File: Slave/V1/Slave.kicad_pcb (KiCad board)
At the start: 2 copper layers, 130.6 x 138.2 mm, 534 parts, among them J101 649002227222, J102 649002227222, J1301 649002227222, J1701 649002227222, J201 Header_Male_Pin_2.54mm_1X6_,_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, J202 Header_Male_Pin_2.54mm_1X3_,_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, J2101 649002227222, J2501 649002227222, J2901 649002227222, J300 Header_Male_Pin_2.54mm_1X2_,_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, J3301 649002227222, J401 649006227222, J402 649006227222, J501 649002227222, J901 649002227222, Q101 2N7002P,215, Q1201 CPH6347-TL-W, Q1202 BSS806NH6327XTSA1, Q1301 CPH6347-TL-W, Q1302 CPH6347-TL-W, Q1601 CPH6347-TL-W, Q1602 BSS806NH6327XTSA1, Q1701 CPH6347-TL-W, Q1702 CPH6347-TL-W, Q2001 CPH6347-TL-W, Q2002 BSS806NH6327XTSA1, Q2101 CPH6347-TL-W, Q2102 CPH6347-TL-W, Q2401 CPH6347-TL-W, Q2402 BSS806NH6327XTSA1, Q2501 CPH6347-TL-W, Q2502 CPH6347-TL-W, Q2801 CPH6347-TL-W, Q2802 BSS806NH6327XTSA1, Q2901 CPH6347-TL-W, Q2902 CPH6347-TL-W, Q3201 CPH6347-TL-W, Q3202 BSS806NH6327XTSA1, Q3301 CPH6347-TL-W, Q3302 CPH6347-TL-W, Q3601 CPH6347-TL-W, Q3602 BSS806NH6327XTSA1, Q501 CPH6347-TL-W, Q502 CPH6347-TL-W, Q801 CPH6347-TL-W, Q802 BSS806NH6327XTSA1, Q901 CPH6347-TL-W, Q902 CPH6347-TL-W, SW201 PTS645SM43SMTR92, SW202 PTS645SM43SMTR92, U1001 AP3015KTR-G1, U1002 AP2202K-ADJTRG1, U1101 ADC121S021CIMF/NOPB, U1201 ADCMP350YKSZ-REEL7, U1301 LTV-816S, U1302 SI8641AB-B-IS1, U1401 AP3015KTR-G1, U1402 AP2202K-ADJTRG1, U1501 ADC121S021CIMF/NOPB, U1601 ADCMP350YKSZ-REEL7, U1701 LTV-816S, U1702 SI8641AB-B-IS1, U1801 AP3015KTR-G1, U1802 AP2202K-ADJTRG1, U1901 ADC121S021CIMF/NOPB, U2001 ADCMP350YKSZ-REEL7, U201 STM32F446RE, U2101 LTV-816S, U2102 SI8641AB-B-IS1, U2201 AP3015KTR-G1, U2202 AP2202K-ADJTRG1, U2301 ADC121S021CIMF/NOPB, U2401 ADCMP350YKSZ-REEL7, U2501 LTV-816S, U2502 SI8641AB-B-IS1, U2601 AP3015KTR-G1, U2602 AP2202K-ADJTRG1, U2701 ADC121S021CIMF/NOPB, U2801 ADCMP350YKSZ-REEL7, U2901 LTV-816S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

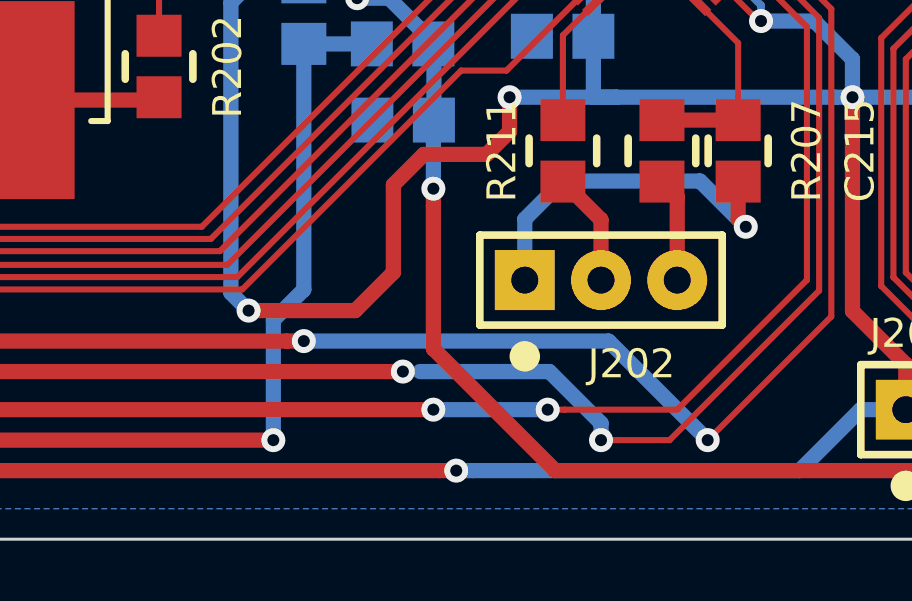
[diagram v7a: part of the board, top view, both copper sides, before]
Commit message: add silkscreen USART2
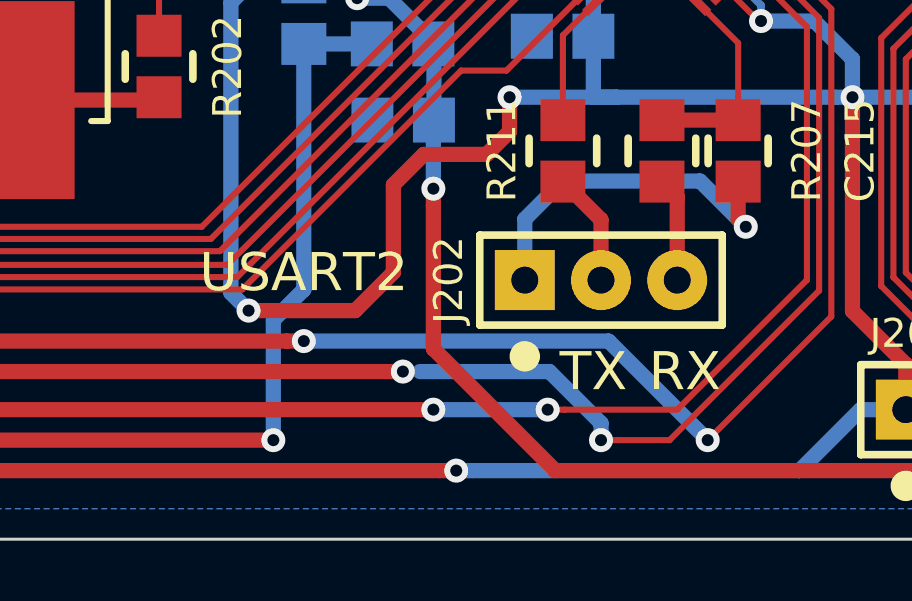
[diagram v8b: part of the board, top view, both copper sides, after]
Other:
- board text added: "RX"
- board text added: "TX"
- board text added: "USART2"
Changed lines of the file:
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@@
     (area 88.087999 39.827999 218.744001 178.104001)
     (thickness 1.6)
-    (drawings 109)
+    (drawings 112)
     (tracks 4363)
     (zones 0)
@@
   (module Connectors:Headers_2.54mm_1X3 (layer F.Cu)
     (at 149.352 169.418)
-    (fp_text reference J202 (at 3.556 2.794 180) (layer F.SilkS)
+    (fp_text reference J202 (at -2.54 0 270) (layer F.SilkS)
       (effects (font (size 0.9652 0.9652) (thickness 0.2032)))
     )
@@
     )
   )
+  (gr_text USART2 (at 141.986 169.164 360) (layer F.SilkS)
+    (effects (font (size 1.27 1.27) (thickness 0.2032)))
+  )
+  (gr_text TX (at 151.638 172.466) (layer F.SilkS)
+    (effects (font (size 1.27 1.27) (thickness 0.2032)))
+  )
+  (gr_text RX (at 154.686 172.466) (layer F.SilkS)
+    (effects (font (size 1.27 1.27) (thickness 0.2032)))
+  )
   (gr_text SWD (at 167.64 170.942) (layer F.SilkS)
